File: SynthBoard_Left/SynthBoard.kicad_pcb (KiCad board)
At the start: 2 copper layers, 155 x 80 mm, 108 parts, among them IC3 PIC16F15325-I/SL, IC4 AS321KTR-G1, IC5 V3340M, IC6 AS321KTR-G1, IC7 HEF4013BT,653, J1 DigiInput, J2 ICSP LFO, J3 D_Power, J4 VCOOut, J6 A_Power, J7 LFO, Q1 2SC1623(RANGE:300-400), Q2 2SC1623(RANGE:300-400), SW1 MFP_240, U1 TJM4558CDT, U7 MCP6234T-E/SL

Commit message: SynthBoard
Rightを配置済
Leftの配線ミスを修正
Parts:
- C51, C52: value CL21C102JBCNNNC -> 0805B103J500NT
- R118: value 0805W8F1801T5E -> 0805W8F1501T5E
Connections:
- R193 pad 1: PWM_S_LFO -> Triangle
- S2 pad 3: PWM_S_LFO -> Triangle
- S2 pad 6: PWM_S_LFO -> Triangle
- VR3 pad 1: GNDA -> +5VA

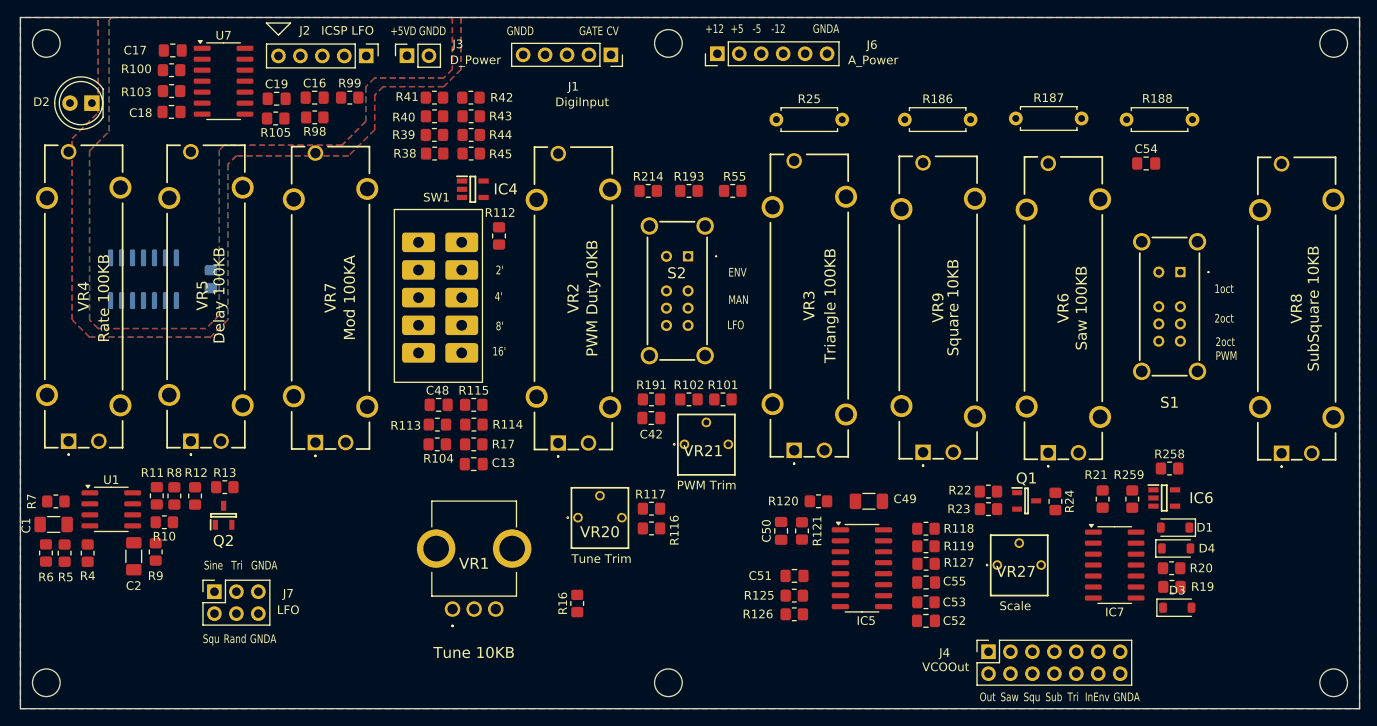
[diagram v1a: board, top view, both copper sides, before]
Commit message: SynthBoard_Left
JLCPCBでBasic部品に置き換えた
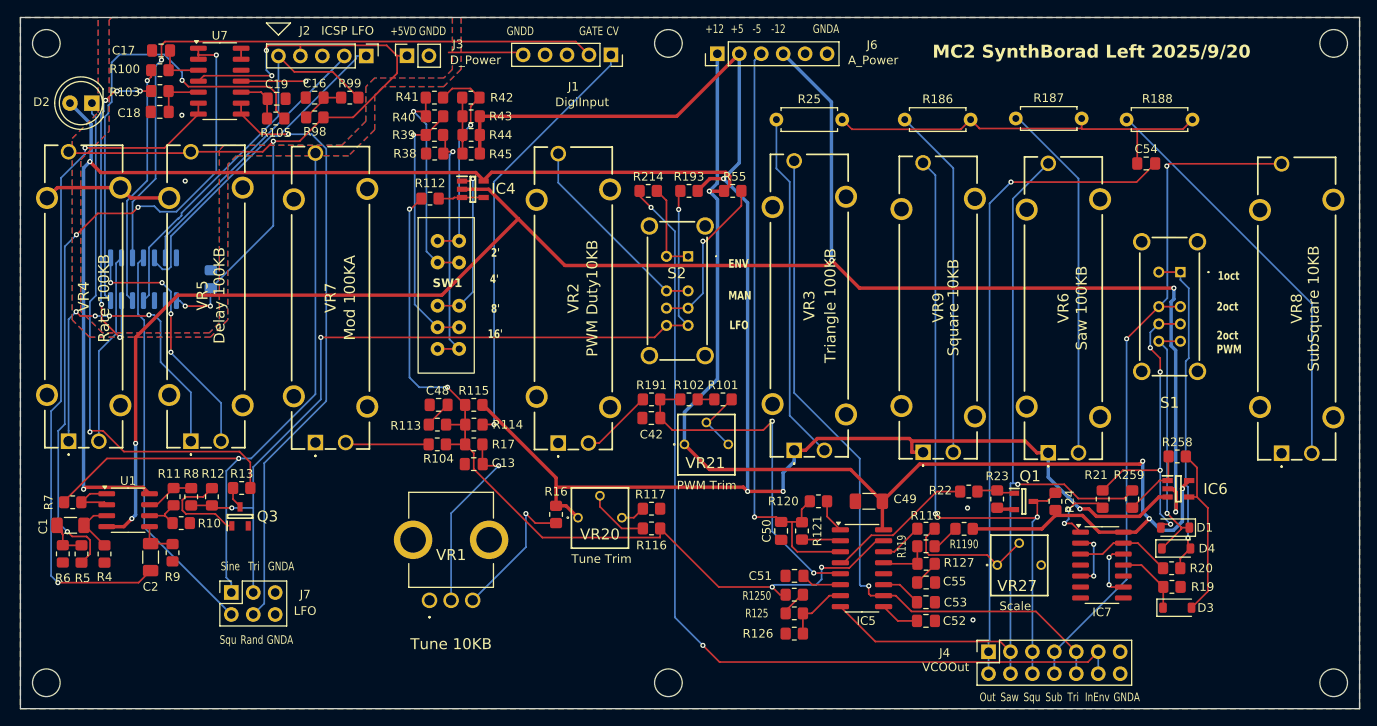
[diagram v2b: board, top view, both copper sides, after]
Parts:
- removed Q2: 2SC1623(RANGE:300-400), SamacSys_parts:SOT95P237X125-3N
- added Q3: SS8050(RANGE:200-350), SamacSys_parts:SOT95P240X115-3N, F.Cu at (66.4, 97.7)
- added R1190: 0805W8F4703T5E, Resistor_SMD:R_0805_2012Metric_Pad1.20x1.40mm_HandSolder, F.Cu at (150.2, 99.2)
- added R1250: 0805W8F4703T5E, Resistor_SMD:R_0805_2012Metric_Pad1.20x1.40mm_HandSolder, F.Cu at (130.6, 106.8)
- C1, C2: value EMK316BBJ476ML-T -> CL31A476MPHNNNE
- C13: value CL21C102JBCNNNC -> CL21B102KBCNNNC
- C16, C17, C18, C19, C42, C48, C51, C52, C55: value 0805B103J500NT -> CL21B103KBANNNC
- C50: value CL21B225KAFNNNE -> CL21A225KBQNNNE
- C53: value CL21C102JBCNNNC -> CL21B102KBCNNNC; footprint Resistor_SMD:R_0805_2012Metric_Pad1.20x1.40mm_HandSolder -> Capacitor_SMD:C_0805_2012Metric_Pad1.18x1.45mm_HandSolder
- Q1: value 2SC1623(RANGE:300-400) -> SS8050(RANGE:200-350); footprint SamacSys_parts:SOT95P237X125-3N -> SamacSys_parts:SOT95P240X115-3N
- R101: value 0805W8J0563T5E -> 0805W8F5102T5E
- R102: value 0805W8J0394T5E -> 0805W8F4703T5E
- R112, R114, R116, R12, R191, R4, R9: value 0805W8J0104T5E -> 0805W8F1003T5E
- R115: value 0805W8F5603T5E -> 0805W8F4703T5E
- R117: value 0805W8F2703T5E -> 0805W8F2203T5E
- R119, R125: value 0805W8F1504T5E -> 0805W8F1004T5E
- R120: value 0805W8F2802T5E -> 0805W8F2702T5E
- R55: value ARG05DTC5002 -> 0805W8F5102T5E
- SW1: value MFP_240 -> MFP_2424; footprint SamacSys_parts:MFP 240 -> SamacSys_parts:MFP 2424
- U1: value TJM4558CDT -> TL072CDT
- moved R16 10.6 mm to (103.0, 97.5)
- moved R112 9.08 mm to (88.4, 61.0), turned to 180 degrees
- moved SW1 6.53 mm to (90.8, 78.9)
- moved VR1 2.85 mm to (88.3, 107.5)
- moved R22 2.27 mm to (150.8, 94.9)
- moved R126 2.24 mm to (130.6, 111.3)
- moved R125 2.05 mm to (130.6, 109.0)
- moved J7 1.95 mm to (65.4, 106.6)
- moved C1 1.95 mm to (46.8, 98.8)
- moved C2 1.95 mm to (56.1, 102.5)
- moved R10 1.95 mm to (59.6, 98.5)
- moved R11 1.95 mm to (58.7, 95.5)
- moved R12 1.95 mm to (63.2, 95.5)
- moved R4 1.95 mm to (50.7, 102.1)
- moved R5 1.95 mm to (48.1, 102.1)
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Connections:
- R119 pad 2: +12VA -> Net-(R119-Pad2)
- R125 pad 1: Vfci -> Net-(R125-Pad1)
- SW1 pad 1: RANGE_C -> RANGE_2
- SW1 pad 10: RANGE_C -> RANGE_2
- SW1 pad 2: RANGE_2 -> RANGE_4
- SW1 pad 3: RANGE_4 -> RANGE_C
- SW1 pad 8: RANGE_4 -> RANGE_C
- SW1 pad 9: RANGE_2 -> RANGE_4
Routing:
- net +12VA: track 0.00 -> 282.0 mm, vias 0 -> 6
- net -12VA: track 0.00 -> 218.0 mm, vias 0 -> 5
- net +5VA: track 0.00 -> 196.4 mm, vias 0 -> 4
- net EnvFlt: track 0.00 -> 105.2 mm, vias 0 -> 2
- net Vfci: track 0.00 -> 100.9 mm, vias 0 -> 4
- net +5VD: track 0.00 -> 100.8 mm, vias 0 -> 5
- net Triangle: track 0.00 -> 99.3 mm, vias 0 -> 3
- net Vso: track 0.00 -> 97.8 mm, vias 0 -> 1
- net Vtri: track 0.00 -> 83.5 mm, vias 0 -> 1
- net SubVP: track 0.00 -> 80.1 mm, vias 0 -> 2
- net Raw_Triangle: track 0.00 -> 79.6 mm, vias 0 -> 2
- net Raw_Sine: track 0.00 -> 78.9 mm, vias 0 -> 4
- net Sine: track 0.00 -> 78.6 mm, vias 0 -> 1
- net Gate: track 0.00 -> 76.3 mm, vias 0 -> 1
- net VPseparate: track 0.00 -> 76.1 mm, vias 0 -> 2
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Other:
- board text added: "MC2 SynthBorad Left 2025/9/20"

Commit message: MC2
まとめて登録
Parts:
- C17, C18, C19: value CL21B103KBANNNC -> GRM21B5C2E103FWAA
- C53: value CL21B102KBCNNNC -> ECH-U1H102GX5
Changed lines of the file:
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@@
 			)
 		)
-		(property "Value" "CL21B103KBANNNC"
+		(property "Value" "GRM21B5C2E103FWAA"
 			(at 0 1.68 0)
 			(layer "F.Fab")
@@
 			)
 		)
-		(property "Value" "CL21B102KBCNNNC"
+		(property "Value" "ECH-U1H102GX5"
 			(at 0 1.68 180)
 			(layer "F.Fab")
@@
 			)
 		)
-		(property "Value" "CL21B103KBANNNC"
+		(property "Value" "GRM21B5C2E103FWAA"
 			(at 0 1.68 0)
 			(layer "F.Fab")
@@
 			)
 		)
-		(property "Value" "CL21B103KBANNNC"
+		(property "Value" "GRM21B5C2E103FWAA"
 			(at 0 1.68 0)
 			(layer "F.Fab")
